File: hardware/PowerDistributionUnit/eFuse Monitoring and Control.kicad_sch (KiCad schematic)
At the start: 74 parts, among them U34 MCP23017_SO, U37 MCP23017_SO, U38 ADS131M08-Q1, U39 ADS131M08-Q1, Y1 ABM3-8.000MHZ-D2Y-T, Y2 ABM3-8.000MHZ-D2Y-T

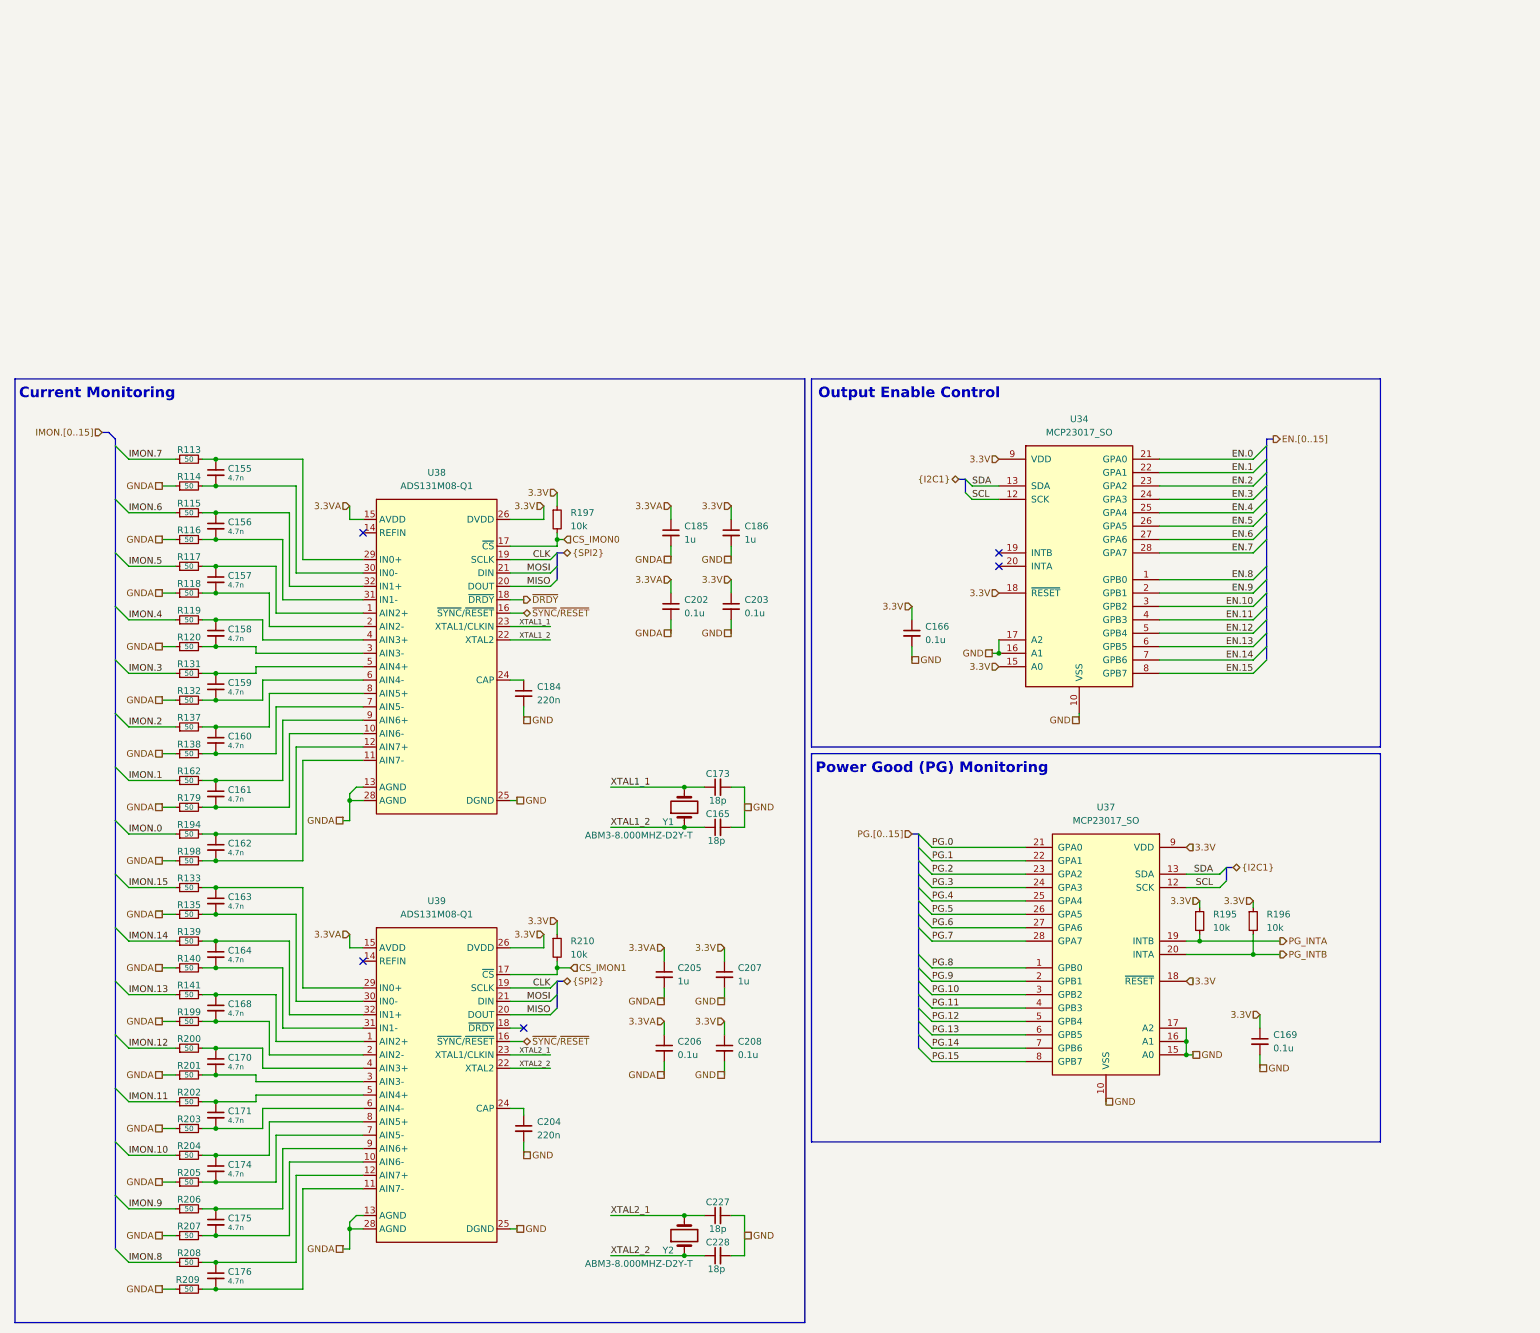
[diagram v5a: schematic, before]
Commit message: GPIO expander for PG and EN routing
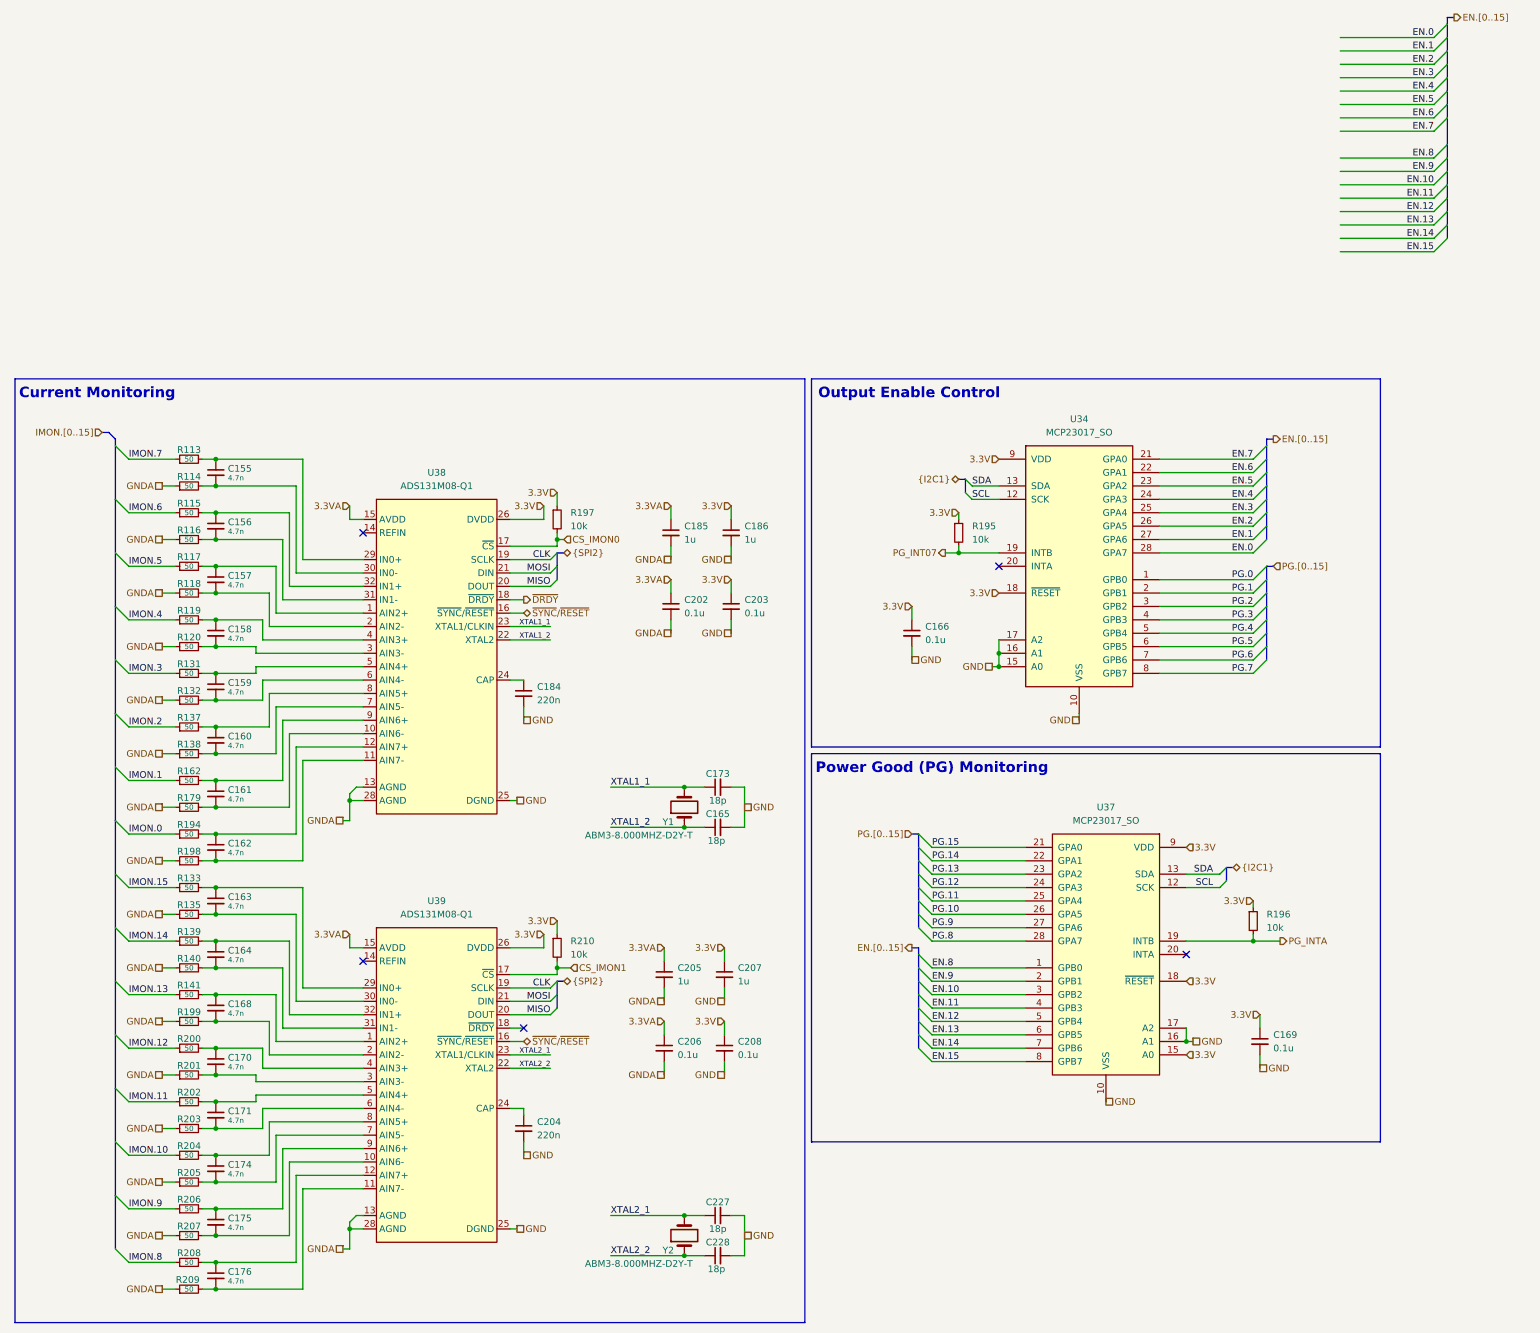
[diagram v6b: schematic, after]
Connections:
- net 3.3V: now also U37.15 (A0); no longer U34.15 (A0)
- net EN.0: now also U34.28 (GPA7); no longer U34.21 (GPA0)
- net EN.1: now also U34.27 (GPA6); no longer U34.22 (GPA1)
- net EN.10: now also U37.3 (GPB2); no longer U34.3 (GPB2)
- net EN.11: now also U37.4 (GPB3); no longer U34.4 (GPB3)
- net EN.12: now also U37.5 (GPB4); no longer U34.5 (GPB4)
- net EN.13: now also U37.6 (GPB5); no longer U34.6 (GPB5)
- net EN.14: now also U37.7 (GPB6); no longer U34.7 (GPB6)
- net EN.15: now also U37.8 (GPB7); no longer U34.8 (GPB7)
- net EN.2: now also U34.26 (GPA5); no longer U34.23 (GPA2)
- net EN.3: now also U34.25 (GPA4); no longer U34.24 (GPA3)
- net EN.4: now also U34.24 (GPA3); no longer U34.25 (GPA4)
- net EN.5: now also U34.23 (GPA2); no longer U34.26 (GPA5)
- net EN.6: now also U34.22 (GPA1); no longer U34.27 (GPA6)
- net EN.7: now also U34.21 (GPA0); no longer U34.28 (GPA7)
- net EN.8: now also U37.1 (GPB0); no longer U34.1 (GPB0)
- net EN.9: now also U37.2 (GPB1); no longer U34.2 (GPB1)
- net GND: now also U34.15 (A0); no longer U37.15 (A0)
- net PG.0: now also U34.1 (GPB0); no longer U37.21 (GPA0)
- net PG.1: now also U34.2 (GPB1); no longer U37.22 (GPA1)
- net PG.10: now also U37.26 (GPA5); no longer U37.3 (GPB2)
- net PG.11: now also U37.25 (GPA4); no longer U37.4 (GPB3)
- net PG.12: now also U37.24 (GPA3); no longer U37.5 (GPB4)
- net PG.13: now also U37.23 (GPA2); no longer U37.6 (GPB5)
- net PG.14: now also U37.22 (GPA1); no longer U37.7 (GPB6)
- net PG.15: now also U37.21 (GPA0); no longer U37.8 (GPB7)
- net PG.2: now also U34.3 (GPB2); no longer U37.23 (GPA2)
- net PG.3: now also U34.4 (GPB3); no longer U37.24 (GPA3)
- net PG.4: now also U34.5 (GPB4); no longer U37.25 (GPA4)
- net PG.5: now also U34.6 (GPB5); no longer U37.26 (GPA5)
- net PG.6: now also U34.7 (GPB6); no longer U37.27 (GPA6)
- net PG.7: now also U34.8 (GPB7); no longer U37.28 (GPA7)
- net PG.8: now also U37.28 (GPA7); no longer U37.1 (GPB0)
- net PG.9: now also U37.27 (GPA6); no longer U37.2 (GPB1)
- net PG_INTA: now also R196.2; no longer R195.2
- net PG_INT07: now reaches U34.19 (INTB)
- net PG_INT07: now also R195.2
- net PG_INTB: no longer names the net of U37.20 (INTA)
- net PG_INTB: no longer R196.2
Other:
- moved on the sheet: R195

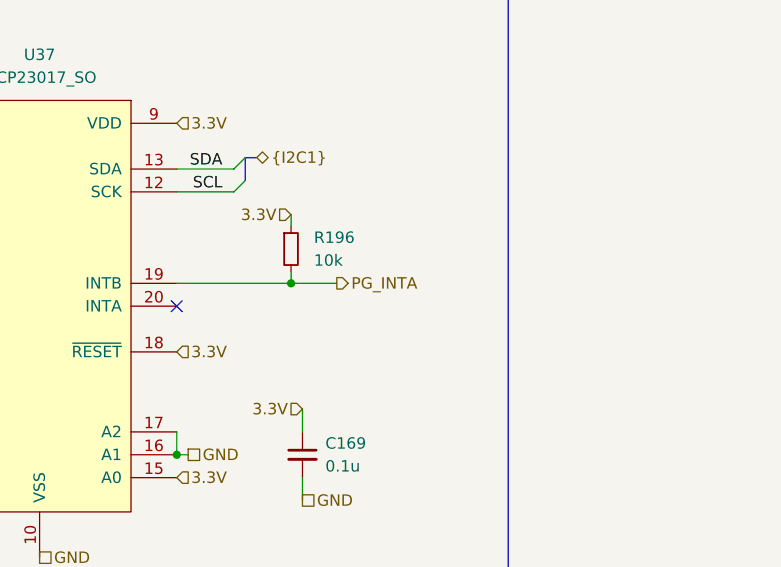
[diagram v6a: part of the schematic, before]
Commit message: test points, gnd net ties (added extra one), fixed drdy/sync mixup
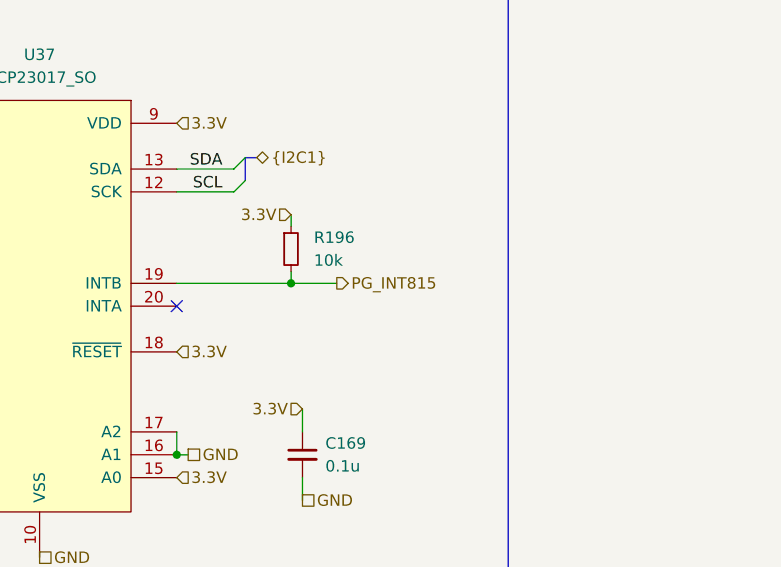
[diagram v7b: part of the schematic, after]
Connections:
- net PG_INTA renamed PG_INT815
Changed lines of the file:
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@@
 		)
 	)
-	(hierarchical_label "PG_INTA"
+	(hierarchical_label "PG_INT815"
 		(shape output)
 		(at 256.54 121.92 0)
